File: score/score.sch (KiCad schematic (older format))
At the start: 23 parts, among them J1 Conn_01x02, P8 CONN_01X07, P9 CONN_01X07, U1 74HC595T16-13, U2 HDSP-C8A1, U3 HDSP-C8A1, U4 HDSP-C8A1, U5 74HC595T16-13, U6 74HC595T16-13, U7 TSR1-2433

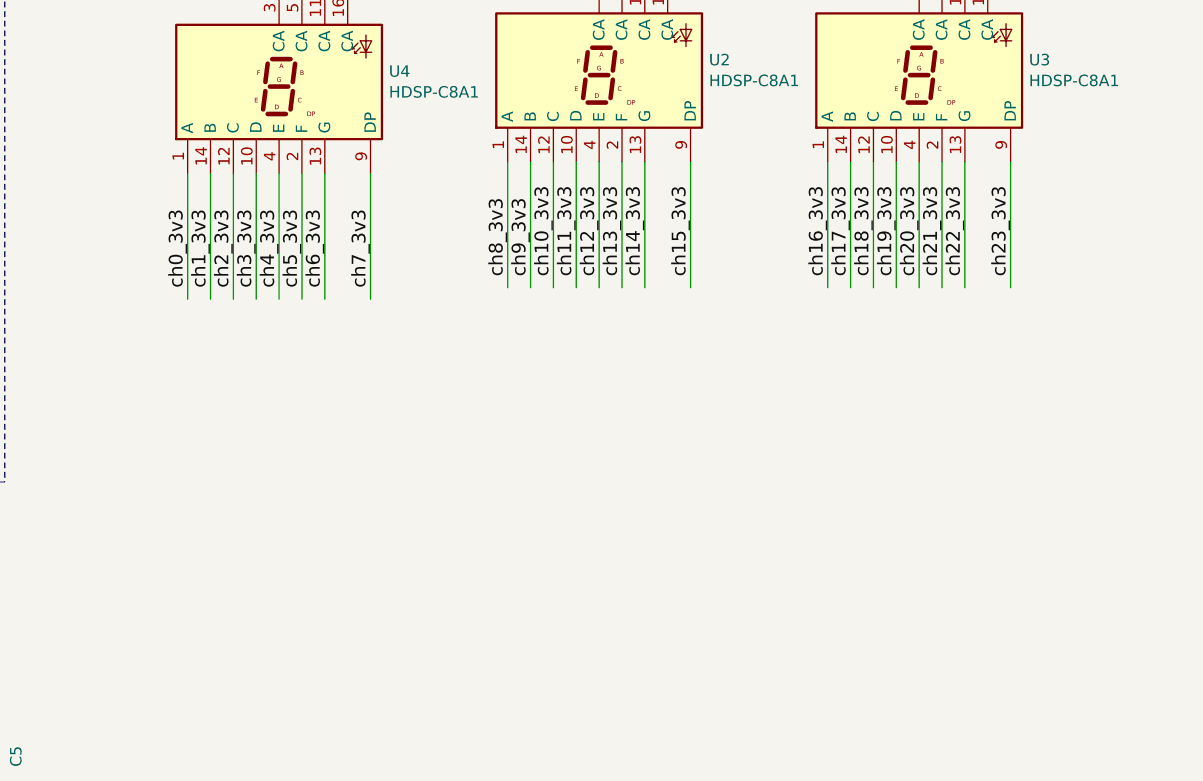
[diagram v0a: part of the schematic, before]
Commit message: resistor added on 7-seg
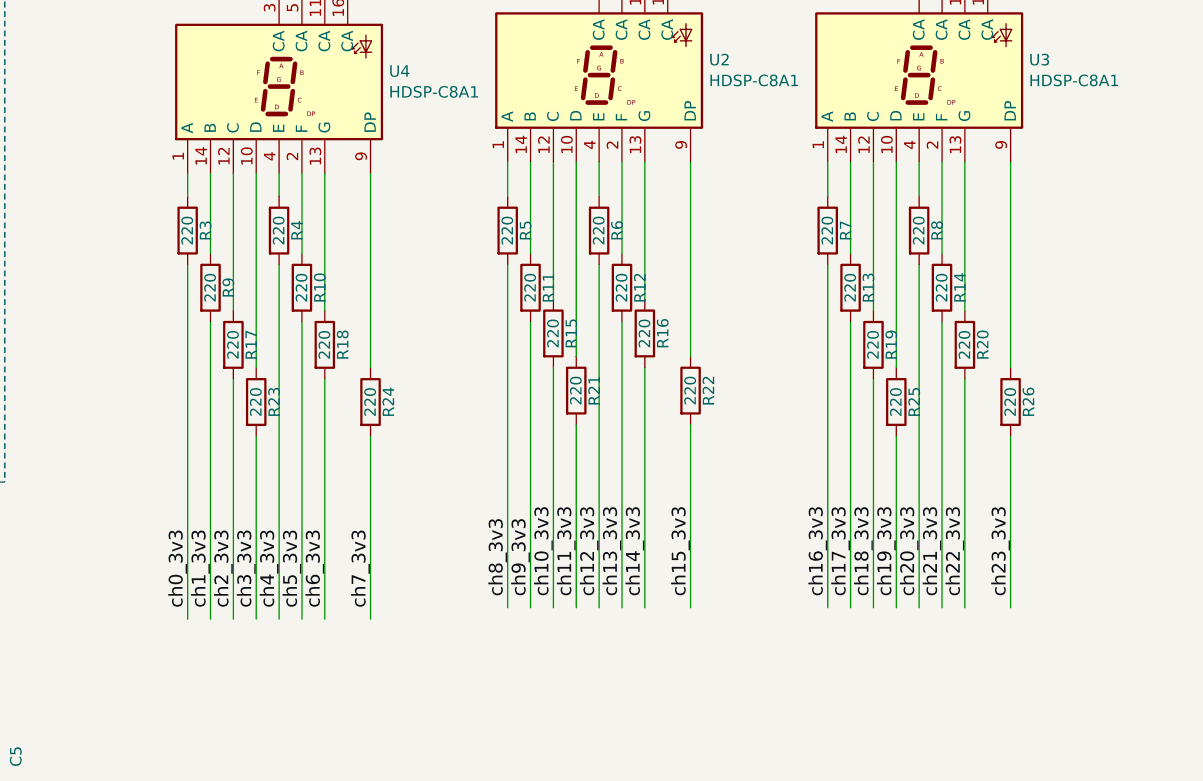
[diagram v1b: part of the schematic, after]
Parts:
- added R10, R11, R12, R13, R14, R15, R16, R17, R18, R19, R20, R21, R22, R23, R24, R25, R26, R3, R4, R5, R6, R7, R8, R9: 220, espitall:R_0603_HandSoldering, symbol device:R
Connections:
- wire segments 162 -> 186

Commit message: score board routed
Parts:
- C1, C2, C3, C4, C5: symbol device:C -> score-rescue:C-device
- J1: symbol conn:Conn_01x02 -> score-rescue:Conn_01x02-conn
- R1, R10, R11, R12, R13, R14, R15, R16, R17, R18, R19, R2, R20, R21, R22, R23, R24, R25, R26, R3, R4, R5, R6, R7, R8, R9: symbol device:R -> score-rescue:R-device
- U1, U5, U6: symbol espitall:74HC595T16-13 -> score-rescue:74HC595T16-13-espitall
- U2, U3, U4: symbol espitall:HDSP-C8A1 -> score-rescue:HDSP-C8A1-espitall
- U7: symbol espitall:TSR1-2433 -> score-rescue:TSR1-2433-espitall
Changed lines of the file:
@@
 $EndComp
 $Comp
-L device:R R1
+L score-rescue:R-device R1
 U 1 1 573CEAA0
 P 6300 1550
@@
 NoConn ~ 9800 1500
 $Comp
-L device:C C1
+L score-rescue:C-device C1
 U 1 1 573CB74D
 P 4450 1900
@@
 	1050 2100 1250 2100
 $Comp
-L espitall:74HC595T16-13 U1
+L score-rescue:74HC595T16-13-espitall U1
 U 1 1 5787DC8B
 P 2250 4050
@@
 NoConn ~ 9800 2000
 $Comp
-L device:C C2
+L score-rescue:C-device C2
 U 1 1 5935296B
 P 2950 3300
@@
 	1550 1700 2550 1700
 $Comp
-L power:GND #PWR01
+L score-rescue:GND-power #PWR01
 U 1 1 5A2F7B7E
 P 1250 2250
@@
 $EndComp
 $Comp
-L power:GND #PWR02
+L score-rescue:GND-power #PWR02
 U 1 1 5A2F7F39
 P 2350 2250
@@
 $EndComp
 $Comp
-L power:+3V3 #PWR03
+L score-rescue:+3V3-power #PWR03
 U 1 1 5A2F8189
 P 1250 1400
@@
 $EndComp
 $Comp
-L power:+3V3 #PWR04
+L score-rescue:+3V3-power #PWR04
 U 1 1 5A2F8279
 P 2350 1400
@@
 $EndComp
 $Comp
-L power:+3V3 #PWR06
+L score-rescue:+3V3-power #PWR06
 U 1 1 5A2F8550
 P 2100 3100
@@
 $EndComp
 $Comp
-L power:+3V3 #PWR07
+L score-rescue:+3V3-power #PWR07
 U 1 1 5A2F8601
 P 2950 3100
@@
 $EndComp
 $Comp
-L power:GND #PWR08
+L score-rescue:GND-power #PWR08
 U 1 1 5A2F86B2
 P 2950 3500
@@
 $EndComp
 $Comp
-L power:+3V3 #PWR09
+L score-rescue:+3V3-power #PWR09
 U 1 1 5A2F879B
 P 4450 1400
@@
 $EndComp
 $Comp
-L power:GND #PWR010
+L score-rescue:GND-power #PWR010
 U 1 1 5A2F88C3
 P 4450 2250
@@
 	4450 1400 4450 1750
 $Comp
-L power:GND #PWR011
+L score-rescue:GND-power #PWR011
 U 1 1 5A31A308
 P 1650 5100
@@
 $EndComp
 $Comp
-L power:GND #PWR012
+L score-rescue:GND-power #PWR012
 U 1 1 5A31A494
 P 2100 5100
@@
 $EndComp
 $Comp
-L espitall:74HC595T16-13 U6
+L score-rescue:74HC595T16-13-espitall U6
 U 1 1 5A31E344
 P 2250 6550
@@
 	2700 7350 3300 7350
 $Comp
-L device:C C4
+L score-rescue:C-device C4
 U 1 1 5A31E368
 P 2950 5800
@@
 	2100 5700 2100 5750
 $Comp
-L power:+3V3 #PWR013
+L score-rescue:+3V3-power #PWR013
 U 1 1 5A31E371
 P 2100 5600
@@
 $EndComp
 $Comp
-L power:+3V3 #PWR014
+L score-rescue:+3V3-power #PWR014
 U 1 1 5A31E377
 P 2950 5600
@@
 $EndComp
 $Comp
-L power:GND #PWR015
+L score-rescue:GND-power #PWR015
 U 1 1 5A31E37D
 P 2950 6000
@@
 $EndComp
 $Comp
-L power:GND #PWR016
+L score-rescue:GND-power #PWR016
 U 1 1 5A31E383
 P 1650 7600
@@
 $EndComp
 $Comp
-L power:GND #PWR017
+L score-rescue:GND-power #PWR017
 U 1 1 5A31E389
 P 2100 7600
@@
 $EndComp
 $Comp
-L espitall:74HC595T16-13 U5
+L score-rescue:74HC595T16-13-espitall U5
 U 1 1 5A31FB0C
 P 4500 4050
@@
 	4950 4850 5550 4850
 $Comp
-L device:C C3
+L score-rescue:C-device C3
 U 1 1 5A31FB30
 P 5200 3300
@@
 	4350 3200 4350 3250
 $Comp
-L power:+3V3 #PWR018
+L score-rescue:+3V3-power #PWR018
 U 1 1 5A31FB39
 P 4350 3100
@@
 $EndComp
 $Comp
-L power:+3V3 #PWR019
+L score-rescue:+3V3-power #PWR019
 U 1 1 5A31FB3F
 P 5200 3100
@@
 $EndComp
 $Comp
-L power:GND #PWR020
+L score-rescue:GND-power #PWR020
 U 1 1 5A31FB45
 P 5200 3500
@@
 $EndComp
 $Comp
-L power:GND #PWR021
+L score-rescue:GND-power #PWR021
 U 1 1 5A31FB4B
 P 3900 5100
@@
 $EndComp
 $Comp
-L power:GND #PWR022
+L score-rescue:GND-power #PWR022
 U 1 1 5A31FB51
 P 4350 5100
@@
 	1450 2700 1450 3850
 $Comp
-L espitall:HDSP-C8A1 U4
+L score-rescue:HDSP-C8A1-espitall U4
 U 1 1 5A33F8B5
 P 7050 3750
@@
 $EndComp
 $Comp
-L espitall:HDSP-C8A1 U2
+L score-rescue:HDSP-C8A1-espitall U2
 U 1 1 5A33F909
 P 8450 3700
@@
 $EndComp
 $Comp
-L espitall:HDSP-C8A1 U3
+L score-rescue:HDSP-C8A1-espitall U3
 U 1 1 5A33F989
 P 9850 3700
@@
 	10250 4100 10250 5000
 $Comp
-L power:+3.3VP #PWR023
+L score-rescue:+3.3VP-power #PWR023
 U 1 1 5A358370
 P 7050 2850
@@
 	7050 3250 7050 3350
 $Comp
-L power:+3.3VP #PWR024
+L score-rescue:+3.3VP-power #PWR024
 U 1 1 5A35FB50
 P 8450 2800
@@
 	8450 3200 8450 3300
 $Comp
-L power:+3.3VP #PWR025
+L score-rescue:+3.3VP-power #PWR025
 U 1 1 5A363C66
 P 9850 2800
@@
 	9850 3200 9850 3300
 $Comp
-L espitall:TSR1-2433 U7
+L score-rescue:TSR1-2433-espitall U7
 U 1 1 5A368415
 P 5000 6550
@@
 $EndComp
 $Comp
-L power:GND #PWR026
+L score-rescue:GND-power #PWR026
 U 1 1 5A368465
 P 5000 7100
@@
 $EndComp
 $Comp
-L conn:Conn_01x02 J1
+L score-rescue:Conn_01x02-conn J1
 U 1 1 5A36864D
 P 4100 6500
@@
 	4600 6500 4300 6500
 $Comp
-L power:GND #PWR028
+L score-rescue:GND-power #PWR028
 U 1 1 5A36CD1F
 P 4500 7100
@@
 	5000 6800 5000 7100
 $Comp
-L power:+3.3VP #PWR029
+L score-rescue:+3.3VP-power #PWR029
 U 1 1 5A37F097
 P 5600 6200
@@
 $EndComp
 $Comp
-L device:C C5
+L score-rescue:C-device C5
 U 1 1 5A37F1F8
 P 5800 6850
@@
 $EndComp
 $Comp
-L power:GND #PWR030
+L score-rescue:GND-power #PWR030
 U 1 1 5A37F308
 P 5800 7100
@@
 $EndComp
 $Comp
-L device:R R2
+L score-rescue:R-device R2
 U 1 1 5A39771C
 P 7000 1550
@@
 	7000 1300 7000 1400
 $Comp
-L power:+3.3VP #PWR032
+L score-rescue:+3.3VP-power #PWR032
 U 1 1 5A39C9B3
 P 7000 1300
@@
 $EndComp
 $Comp
-L device:R R3
+L score-rescue:R-device R3
 U 1 1 5A5B03EC
 P 6650 4400
@@
 	6650 4550 6650 6100
 $Comp
-L device:R R9
+L score-rescue:R-device R9
 U 1 1 5A5BC618
 P 6750 4650
@@
 	6750 4800 6750 6100
 $Comp
-L device:R R17
+L score-rescue:R-device R17
 U 1 1 5A5BC65E
 P 6850 4900
@@
 	6850 5050 6850 6100
 $Comp
-L device:R R23
+L score-rescue:R-device R23
 U 1 1 5A5C8B4F
 P 6950 5150
@@
 	6950 5300 6950 6100
 $Comp
-L device:R R4
+L score-rescue:R-device R4
 U 1 1 5A5DBA06
 P 7050 4400
@@
 	7050 4550 7050 6100
 $Comp
-L device:R R10
+L score-rescue:R-device R10
 U 1 1 5A5DBA72
 P 7150 4650
@@
 	7150 4800 7150 6100
 $Comp
-L device:R R18
+L score-rescue:R-device R18
 U 1 1 5A5DBAD4
 P 7250 4900
@@
 	7250 5050 7250 6100
 $Comp
-L device:R R24
+L score-rescue:R-device R24
 U 1 1 5A5DBB52
 P 7450 5150
@@
 	7450 5300 7450 6100
 $Comp
-L device:R R5
+L score-rescue:R-device R5
 U 1 1 5A5DBBBA
 P 8050 4400
@@
 	8050 4550 8050 6050
 $Comp
-L device:R R11
+L score-rescue:R-device R11
 U 1 1 5A5DBC3E
 P 8150 4650
@@
 	8150 4800 8150 6050
 $Comp
-L device:R R15
+L score-rescue:R-device R15
 U 1 1 5A5DBCC6
 P 8250 4850
@@
 	8250 5000 8250 6050
 $Comp
-L device:R R21
+L score-rescue:R-device R21
 U 1 1 5A5DBD46
 P 8350 5100
@@
 	8350 5250 8350 6050
 $Comp
-L device:R R6
+L score-rescue:R-device R6
 U 1 1 5A5DBDD4
 P 8450 4400
@@
 	8450 4550 8450 6050
 $Comp
-L device:R R12
+L score-rescue:R-device R12
 U 1 1 5A5DBE44
 P 8550 4650
@@
 	8550 4800 8550 6050
 $Comp
-L device:R R16
+L score-rescue:R-device R16
 U 1 1 5A5DBEB0
 P 8650 4850
@@
 	8650 5000 8650 6050
 $Comp
-L device:R R22
+L score-rescue:R-device R22
 U 1 1 5A5DBF26
 P 8850 5100
@@
 	8850 5250 8850 6050
 $Comp
-L device:R R7
+L score-rescue:R-device R7
 U 1 1 5A5DBF9E
 P 9450 4400
@@
 	9450 4550 9450 6050
 $Comp
-L device:R R13
+L score-rescue:R-device R13
 U 1 1 5A5DC030
 P 9550 4650
@@
 	9550 4800 9550 6050
 $Comp
-L device:R R19
+L score-rescue:R-device R19
 U 1 1 5A5DC0BC
 P 9650 4900
@@
 	9650 5050 9650 6050
 $Comp
-L device:R R25
+L score-rescue:R-device R25
 U 1 1 5A5DC14A
 P 9750 5150
@@
 	9750 5300 9750 6050
 $Comp
-L device:R R8
+L score-rescue:R-device R8
 U 1 1 5A5DC1CC
 P 9850 4400
@@
 	9850 4550 9850 6050
 $Comp
-L device:R R14
+L score-rescue:R-device R14
 U 1 1 5A5DC246
 P 9950 4650
@@
 	9950 4800 9950 6050
 $Comp
-L device:R R20
+L score-rescue:R-device R20
 U 1 1 5A5DC2C0
 P 10050 4900
@@
 	10050 5050 10050 6050
 $Comp
-L device:R R26
+L score-rescue:R-device R26
 U 1 1 5A5DC34A
 P 10250 5150
